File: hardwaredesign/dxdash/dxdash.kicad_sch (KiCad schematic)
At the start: 5 parts, among them J11 spare, J2 Conn_01x08_Pin

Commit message: controller board added features
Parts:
- removed H1, H2, H3: MountingHole, MountingHole:MountingHole_3.2mm_M3, symbol Mechanical:MountingHole
- removed J11: spare, Connector_PinHeader_2.54mm:PinHeader_1x06_P2.54mm_Vertical, symbol Connector:Conn_01x06_Pin
- removed J2: Conn_01x08_Pin, Connector_PinHeader_2.54mm:PinHeader_1x08_P2.54mm_Vertical, symbol Connector:Conn_01x08_Pin
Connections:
- no-connect marks 6 -> 0
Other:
- removed sheet spareArea
- added sheet bus (bus.kicad_sch)
- added sheet spare (spare.kicad_sch)
- note added: "todo: joystick"
- note removed: "todo: bus wakeup circuit"
- note removed: "todo: buttons, joystick"
- note removed: "todo: display connector, display mounting holes"
- note removed: "todo: dual poti input"
- note removed: "todo: power on/off circuit"

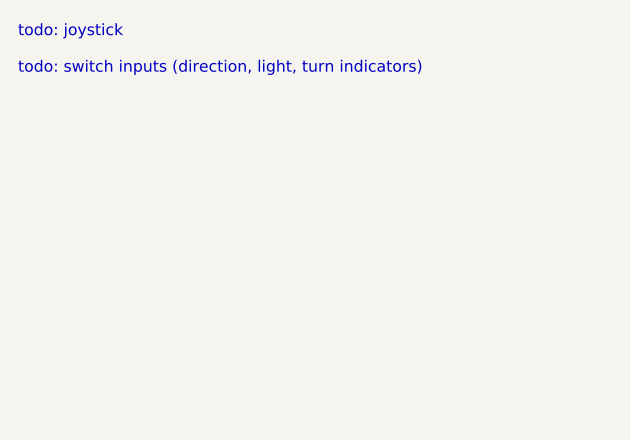
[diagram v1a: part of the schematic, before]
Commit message: added joystick
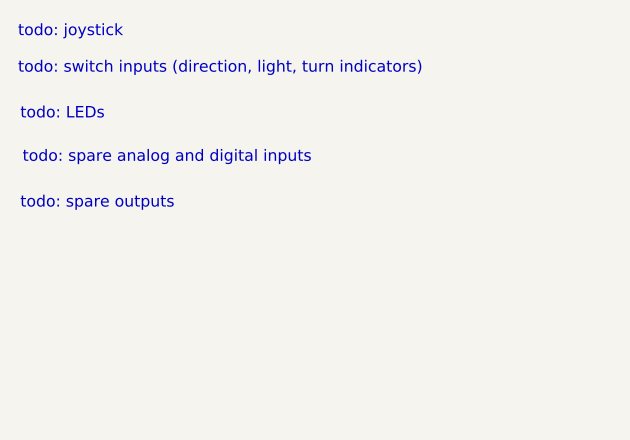
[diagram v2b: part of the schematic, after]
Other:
- note added: "todo: LEDs"
- note added: "todo: spare analog and digital inputs"
- note added: "todo: spare outputs"
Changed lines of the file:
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@@
 		(rev "2")
+	)
+	(text "todo: spare outputs"
+		(exclude_from_sim no)
+		(at 44.45 100.33 0)
+		(effects
+			(font
+				(size 1.27 1.27)
+			)
+			(justify left bottom)
+		)
 	)
 	(text "todo: joystick"
@@
 		(effects
 			(font
+				(size 1.27 1.27)
+			)
+			(justify left bottom)
+		)
+	)
+	(text "todo: LEDs"
+		(exclude_from_sim no)
+		(at 44.45 90.424 0)
+		(effects
+			(font
+				(size 1.27 1.27)
+			)
+			(justify left bottom)
+		)
+	)
+	(text "todo: spare analog and digital inputs"
+		(exclude_from_sim no)
+		(at 44.704 95.25 0)
+		(effects
+			(font

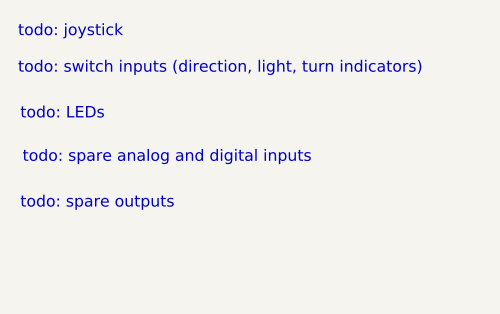
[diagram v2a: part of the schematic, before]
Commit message: added polyfuses
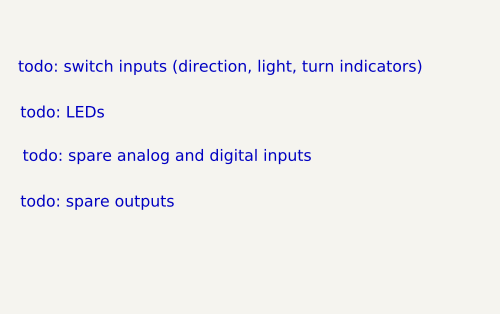
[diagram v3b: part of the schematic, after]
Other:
- note removed: "todo: joystick"
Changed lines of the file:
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@@
-		)
-	)
-	(text "todo: joystick"
-		(exclude_from_sim no)
-		(at 44.196 81.28 0)
-		(effects
-			(font
-				(size 1.27 1.27)
-			)
-			(justify left bottom)
 		)
 	)

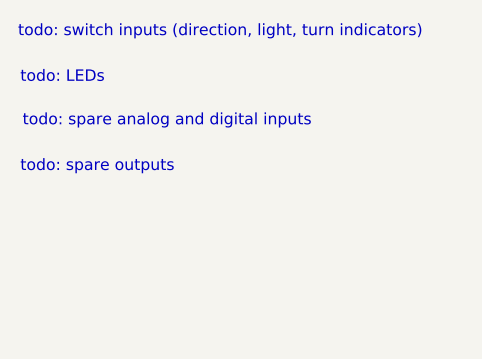
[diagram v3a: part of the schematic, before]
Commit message: added switch inputs. Layout preparation.
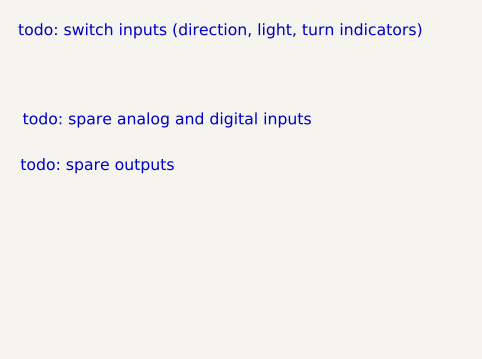
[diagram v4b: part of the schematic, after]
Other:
- note removed: "todo: LEDs"
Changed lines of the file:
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@@
-		)
-	)
-	(text "todo: LEDs"
-		(exclude_from_sim no)
-		(at 44.45 90.424 0)
-		(effects
-			(font
-				(size 1.27 1.27)
-			)
-			(justify left bottom)
 		)
 	)

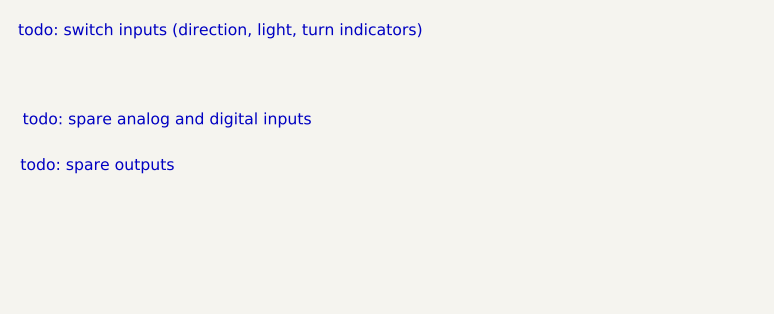
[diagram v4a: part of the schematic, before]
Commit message: board: layout finished
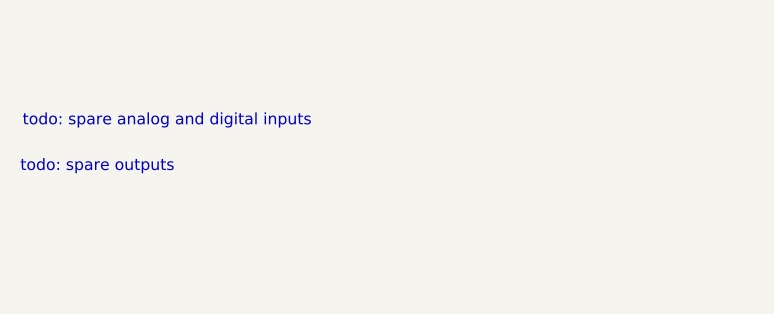
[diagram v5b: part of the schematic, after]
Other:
- note removed: "todo: switch inputs (direction, light, turn indicators)"
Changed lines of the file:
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@@
-		)
-	)
-	(text "todo: switch inputs (direction, light, turn indicators)"
-		(exclude_from_sim no)
-		(at 44.196 85.344 0)
-		(effects
-			(font
-				(size 1.27 1.27)
-			)
-			(justify left bottom)
 		)
 	)

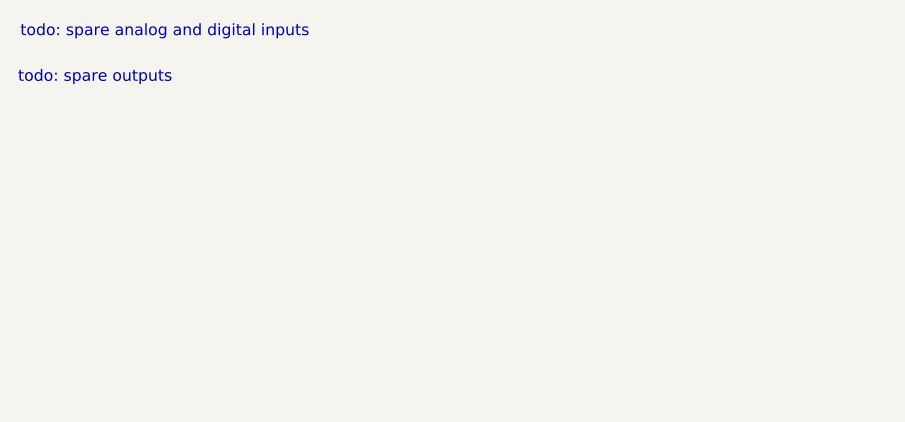
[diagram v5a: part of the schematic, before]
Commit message: dxdash: corrected some resistor values. Added todos.
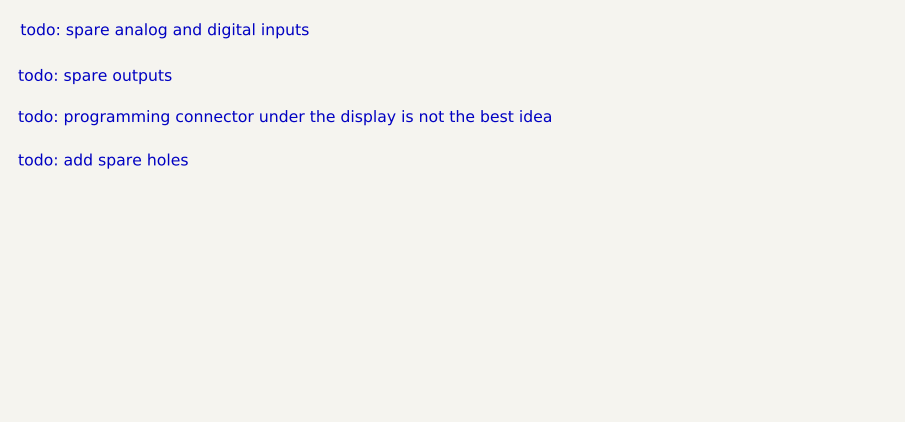
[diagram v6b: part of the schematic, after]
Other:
- note added: "todo: add spare holes"
- note added: "todo: programming connector under the display is not the best idea"
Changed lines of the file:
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@@
 		(rev "2")
+	)
+	(text "todo: programming connector under the display is not the best idea"
+		(exclude_from_sim no)
+		(at 44.45 104.902 0)
+		(effects
+			(font
+				(size 1.27 1.27)
+			)
+			(justify left bottom)
+		)
 	)
 	(text "todo: spare outputs"
@@
 		(effects
 			(font
+				(size 1.27 1.27)
+			)
+			(justify left bottom)
+		)
+	)
+	(text "todo: add spare holes"
+		(exclude_from_sim no)
+		(at 44.45 109.728 0)
+		(effects
+			(font

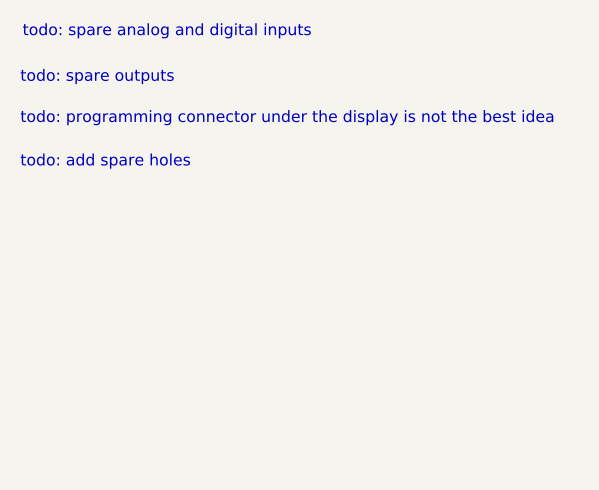
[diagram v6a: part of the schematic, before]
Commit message: gen2: integrated hardwareabstraction, scheduler, buttons, powremanager, turnIndicator
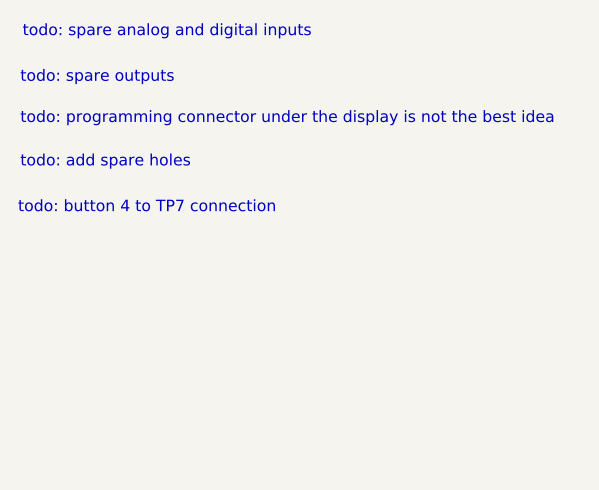
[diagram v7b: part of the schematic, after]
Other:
- note added: "todo: button 4 to TP7 connection"
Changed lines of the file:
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@@
+		)
+	)
+	(text "todo: button 4 to TP7 connection"
+		(exclude_from_sim no)
+		(at 44.196 114.808 0)
+		(effects
+			(font
+				(size 1.27 1.27)
+			)
+			(justify left bottom)
 		)
 	)

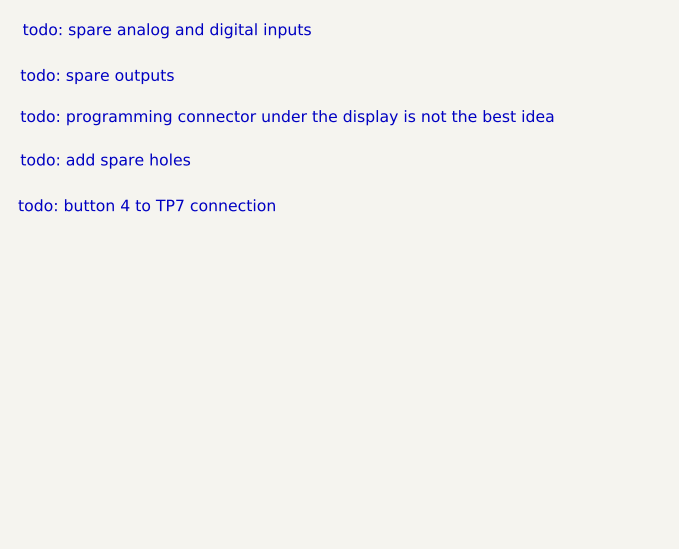
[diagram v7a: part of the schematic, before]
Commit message: added analog inputs. Show analog and buttons on status page.
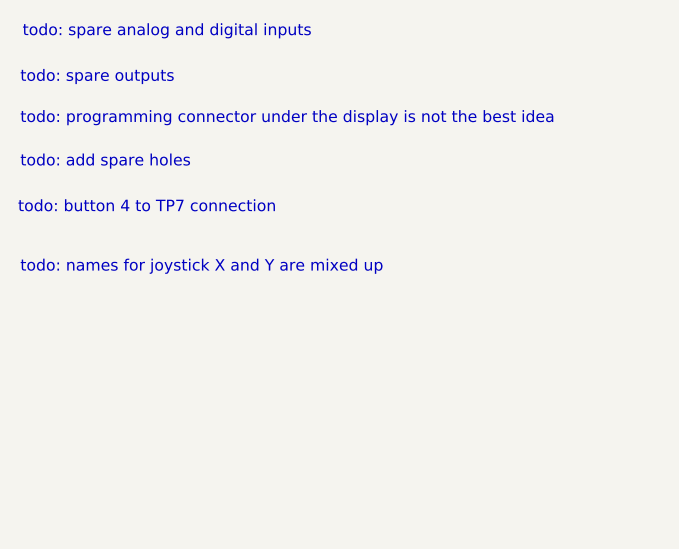
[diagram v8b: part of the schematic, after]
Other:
- note added: "todo: names for joystick X and Y are mixed up"
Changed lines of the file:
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@@
+		)
+	)
+	(text "todo: names for joystick X and Y are mixed up"
+		(exclude_from_sim no)
+		(at 44.45 121.412 0)
+		(effects
+			(font
+				(size 1.27 1.27)
+			)
+			(justify left bottom)
 		)
 	)
